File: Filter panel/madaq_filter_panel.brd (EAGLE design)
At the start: 70.6 x 38.2 mm, 34 parts

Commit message: Filter panel - V4 board (final?)
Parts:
- moved TP2 4.05 mm to (32.7, 53.3)
- moved TP1 2.61 mm to (29.0, 62.5)
- moved C6 2.43 mm to (62.6, 61.4)
- moved R1 2.04 mm to (62.6, 58.8)
- moved C5 1.84 mm to (62.7, 56.2)
- moved JP4 1.84 mm to (35.6, 57.4)
- moved JP3 1.72 mm to (32.6, 57.4)
- moved R2 1.65 mm to (62.7, 53.6)
- moved JP2 1.61 mm to (20.7, 57.4)
- moved JP1 1.52 mm to (23.9, 57.4)
- moved JP6 1.41 mm to (45.5, 57.4)
- moved TP3 1.41 mm to (39.6, 53.3)
- moved JP5 1.41 mm to (42.3, 57.4)
- moved BNC_3 0.91 mm to (24.3, 45.0)
- moved BNC_2 0.77 mm to (60.7, 45.0)
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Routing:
- net N$7: track 13.9 -> 21.3 mm
- net DAC_1: track 100.5 -> 95.1 mm
- net IN-4_B: track 11.1 -> 8.39 mm
- net -5V: track 35.9 -> 38.1 mm
- net IN-1_A: track 11.0 -> 9.06 mm
- net IN-0_A: track 11.0 -> 9.18 mm
- net SW_COM: track 41.5 -> 43.1 mm
- net SIG_1: track 22.0 -> 23.5 mm
- net GND: track 0.00 -> 1.39 mm
- net N$9: track 6.12 -> 7.50 mm
- net IN-2_A: track 8.75 -> 7.50 mm
- net DAC_2: track 3.38 -> 4.58 mm
- net SIG_2: track 32.5 -> 31.4 mm
- net N$8: track 12.4 -> 13.5 mm
- net N$3: track 8.24 -> 9.09 mm
- added copper zone on layer 16, net GND
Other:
- board size 70.6 x 38.2 mm -> 71.1 x 38.2 mm
- board text added: "2015"
- board text added: "DAC2"
- board text added: "DBG"
- board text added: "EXT"
- board text added: "IN0"
- board text added: "IN1"
- board text added: "IN2"
- board text added: "IN4"
- board text added: "INT"

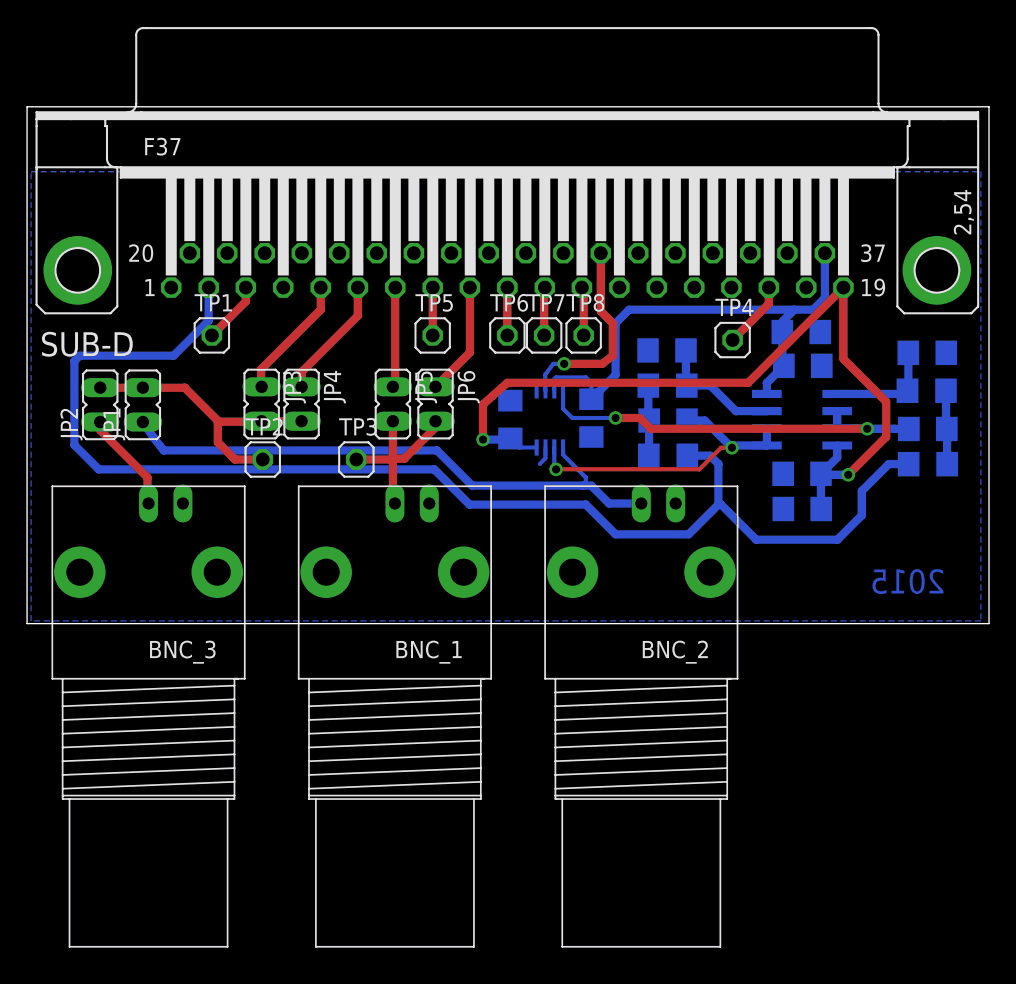
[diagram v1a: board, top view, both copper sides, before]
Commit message: Filter panel - V4 sch + brd, Robi és János átnézte - ez nem a megrendelt verzió (János még babrált a board-on)
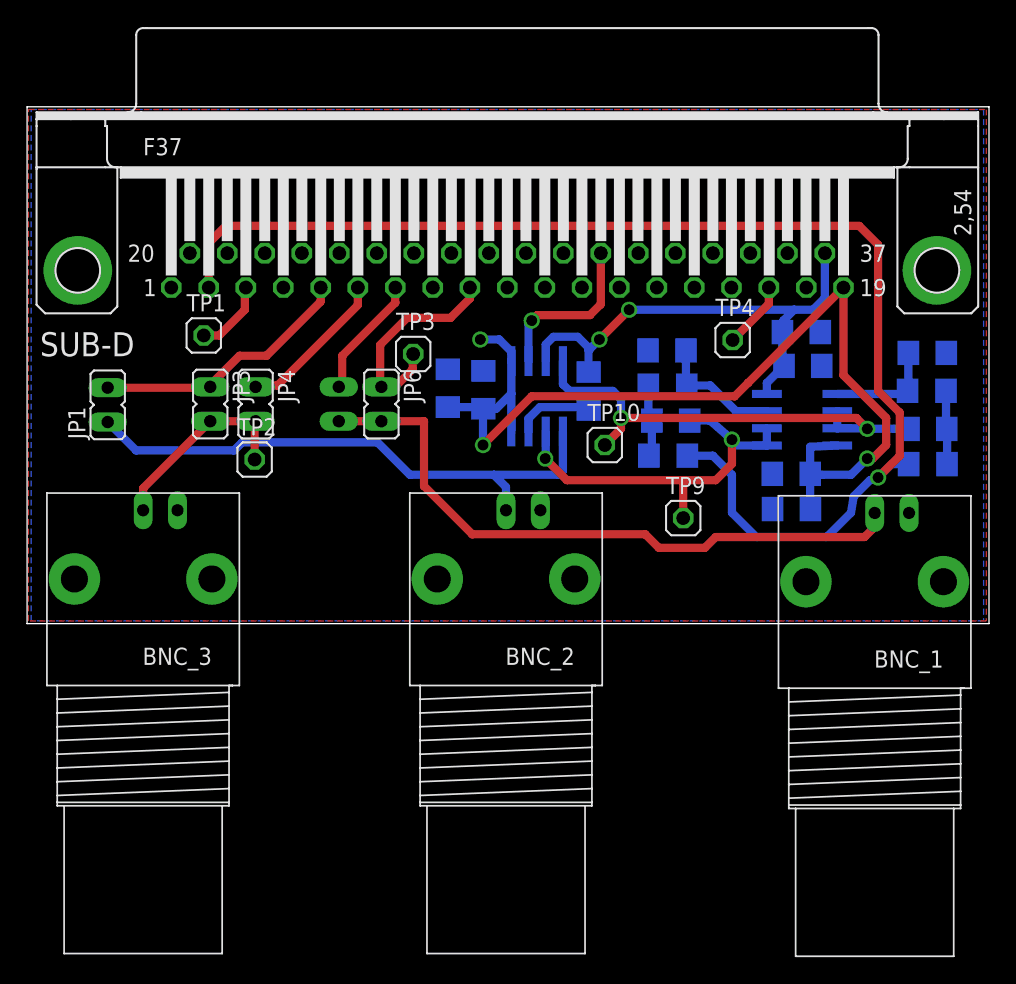
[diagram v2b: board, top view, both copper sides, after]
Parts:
- removed JP2: (no value), jumper:JP1
- removed SWITCH: TS12A12511, Zoli2_2015-02-22:MSOP08
- removed TP5, TP6, TP7, TP8: TP, MRobi:JP1
- added C11: 0.1 uF, Zoli2_2015-01-28:C1206
- added IC1: (no value), MRobi:SO08
- added TP10, TP9: TP, MRobi:JP1
- moved BNC_1 35.5 mm to (78.0, 44.3)
- moved BNC_2 10.0 mm to (50.7, 44.5)
- moved TP3 8.86 mm to (43.8, 61.1)
- moved JP5 4.00 mm to (38.3, 57.4), flipped to the bottom
- moved JP6 4.00 mm to (41.5, 57.4)
- moved JP3 3.80 mm to (28.8, 57.4)
- moved JP4 3.40 mm to (32.2, 57.4)
- moved C9 2.97 mm to (49.0, 58.5)
- moved JP1 2.60 mm to (21.3, 57.4)
- moved C10 2.01 mm to (56.8, 58.4)
- moved C1 0.80 mm to (71.8, 49.7)
- moved C2 0.80 mm to (71.8, 52.3)
- moved BNC_3 0.64 mm to (23.9, 44.5)
- moved TP1 0.60 mm to (28.4, 62.5)
- moved TP2 0.60 mm to (32.1, 53.3)
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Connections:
- removed net N$2: SWITCH.5
- removed net N$7: JP1.2, JP2.2, JP3.2, JP4.2, TP2.1
- net +5V: now also C11.2, IC1.4, IC1.5; no longer SWITCH.4
- net -5V: now also IC1.7; no longer SWITCH.7
- net GND: now also C11.1, IC1.3; no longer SWITCH.3
- net IN-0_A: now also JP1.2
- net IN-3_A: no longer TP5.1
- net IN-4_B: now also TP3.1
- net IN-5_B: no longer TP6.1
- net IN-6_B: no longer TP7.1
- net IN-7_B: no longer TP8.1
- net N$8: no longer TP3.1
- net N$9: now also JP3.2, JP4.2, TP2.1; no longer JP2.1
- net SIG_1: now also IC1.2, TP9.1; no longer SWITCH.2
- net SIG_2: now also IC1.8, TP10.1; no longer SWITCH.8
- net SW_CNTRL: now also IC1.6; no longer SWITCH.6
- net SW_COM: now also IC1.1; no longer SWITCH.1
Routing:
- net N$8: track 13.5 -> 48.0 mm
- net N$7: track 21.3 -> 0.00 mm
- net +5V: track 60.6 -> 74.0 mm, vias 2 -> 3
- net IN-0_A: track 9.18 -> 19.5 mm
- net IN-4_B: track 8.39 -> 16.0 mm
- net N$9: track 7.50 -> 14.8 mm
- net SIG_1: track 23.5 -> 29.4 mm
- net GND: track 1.39 -> 5.84 mm
- net SIG_2: track 31.4 -> 35.8 mm
- net IN-7_B: track 3.59 -> 0.00 mm
- net IN-6_B: track 3.56 -> 0.00 mm
- net IN-3_A: track 3.54 -> 0.00 mm
- net IN-5_B: track 3.54 -> 0.00 mm
- net IN-1_A: track 9.06 -> 11.4 mm
- net SW_CNTRL: track 14.7 -> 12.5 mm
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- added copper zone on layer 1, net GND
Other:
- board text added: "IN"
- board text added: "LP1"
- board text added: "LP2"
- board text added: "OUT"
- board text removed: "2015"

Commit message: Filter panel - János upgraded version, R C értékek még kellenek
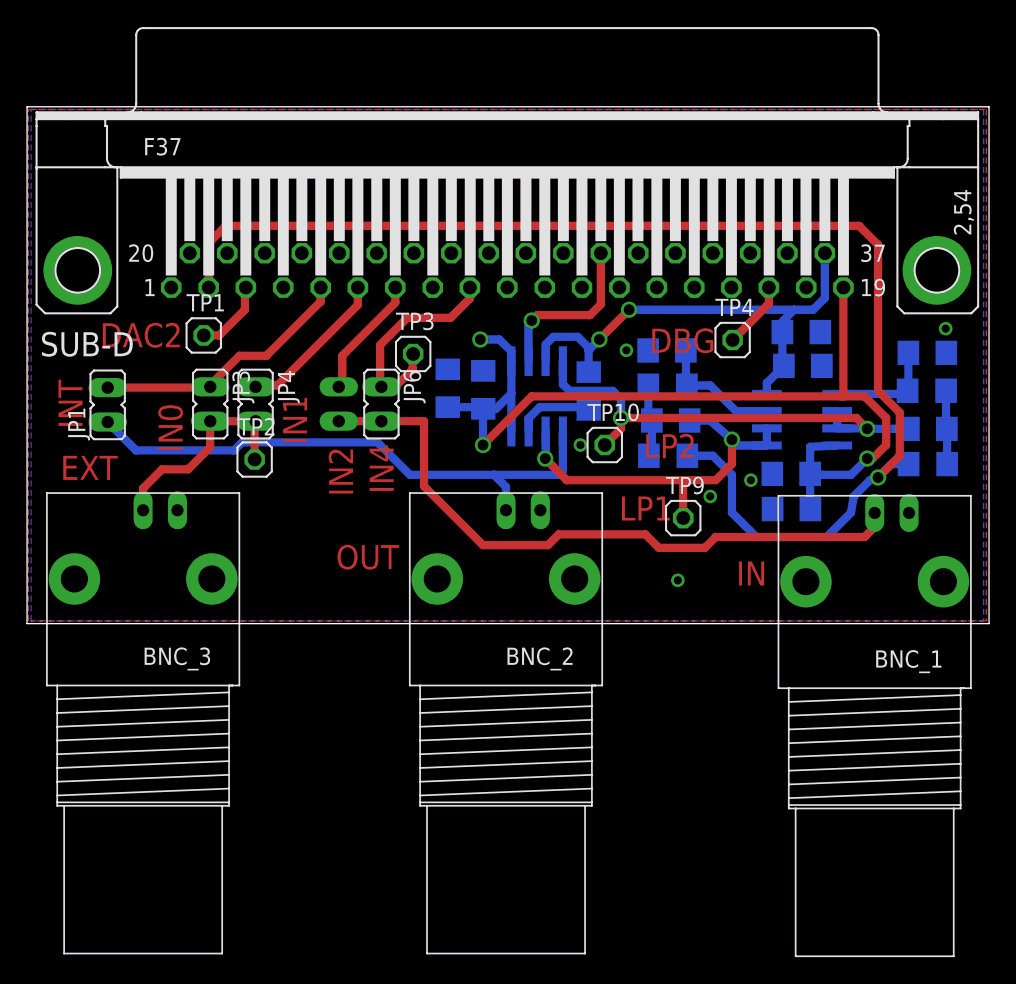
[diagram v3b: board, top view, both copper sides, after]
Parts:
- C1, C2, C3, C4: value (none) -> 100n
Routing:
- net +5V: track 74.0 -> 71.6 mm
- net N$9: track 14.8 -> 16.0 mm
- net N$8: track 48.0 -> 48.6 mm
- net GND: vias 0 -> 6
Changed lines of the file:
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@@
 <wire x1="86.4" y1="41.2" x2="86.4" y2="79.4" width="0" layer="20"/>
 <wire x1="15.3" y1="79.4" x2="15.3" y2="41.2" width="0" layer="20"/>
-<text x="26.8" y="63.4" size="1.778" layer="49" font="vector" rot="R180">DAC2</text>
-<text x="19.4" y="55.6" size="1.778" layer="49" font="vector" rot="R90">INT</text>
-<text x="26.8" y="55.4" size="1.778" layer="49" font="vector" rot="R90">IN0</text>
-<text x="35.8" y="55.6" size="1.778" layer="49" font="vector" rot="R90">IN1</text>
-<text x="39.4" y="60.4" size="1.778" layer="49" font="vector" rot="R90">IN2</text>
-<text x="66.2" y="63" size="1.778" layer="49" font="vector" rot="R180">DBG</text>
-<text x="42.4" y="60.4" size="1.778" layer="49" font="vector" rot="R90">IN4</text>
-<text x="22" y="53.6" size="1.778" layer="49" font="vector" rot="R180">EXT</text>
-<text x="73.4" y="53" size="1.778" layer="49" font="vector" rot="R180">IN</text>
-<text x="48.8" y="53.4" size="1.778" layer="49" font="vector" rot="R180">OUT</text>
+<text x="26.8" y="63.4" size="1.778" layer="1" font="vector" rot="R180">DAC2</text>
+<text x="19.4" y="55.6" size="1.778" layer="1" font="vector" rot="R90">INT</text>
+<text x="26.8" y="53.8" size="1.778" layer="1" font="vector" rot="R90">IN0</text>
+<text x="36" y="54.4" size="1.778" layer="1" font="vector" rot="R90">IN1</text>
+<text x="39.4" y="50.6" size="1.778" layer="1" font="vector" rot="R90">IN2</text>
+<text x="66.2" y="63" size="1.778" layer="1" font="vector" rot="R180">DBG</text>
+<text x="42.4" y="50.8" size="1.778" layer="1" font="vector" rot="R90">IN4</text>
+<text x="22" y="53.6" size="1.778" layer="1" font="vector" rot="R180">EXT</text>
+<text x="70" y="45.8" size="1.778" layer="1" font="vector" rot="R180">IN</text>
+<text x="42.8" y="47" size="1.778" layer="1" font="vector" rot="R180">OUT</text>
 <wire x1="15.3" y1="79.4" x2="86.4" y2="79.4" width="0" layer="20"/>
-<text x="64.8" y="55.2" size="1.778" layer="49" font="vector" rot="R180">LP2</text>
-<text x="66.8" y="47.4" size="1.778" layer="49" font="vector" rot="R180">LP1</text>
+<text x="64.8" y="55.2" size="1.778" layer="1" font="vector" rot="R180">LP2</text>
+<text x="63" y="50.6" size="1.778" layer="1" font="vector" rot="R180">LP1</text>
 </plain>
 <attributes>
@@
 <element name="BNC_2" library="Zoli2_2015-01-28" package="BNCPCB90I" value="" x="50.7" y="44.5" rot="R180"/>
 <element name="BNC_3" library="Zoli2_2015-01-28" package="BNCPCB90I" value="" x="23.88" y="44.5" rot="R180"/>
-<element name="C1" library="Zoli2_2015-01-28" package="C1206" value="" x="71.8" y="49.67" rot="MR180"/>
+<element name="C1" library="Zoli2_2015-01-28" package="C1206" value="100n" x="71.8" y="49.67" rot="MR180"/>
 <element name="C10" library="Zoli2_2015-01-28" package="C1206" value="0.1 uF" x="56.81" y="58.39" rot="MR90"/>
-<element name="C2" library="Zoli2_2015-01-28" package="C1206" value="" x="71.78" y="52.27" rot="MR180"/>
-<element name="C3" library="Zoli2_2015-01-28" package="C1206" value="" x="72.53" y="62.75" rot="MR180"/>
-<element name="C4" library="Zoli2_2015-01-28" package="C1206" value="" x="72.64" y="60.25" rot="MR180"/>
+<element name="C2" library="Zoli2_2015-01-28" package="C1206" value="100n" x="71.78" y="52.27" rot="MR180"/>
+<element name="C3" library="Zoli2_2015-01-28" package="C1206" value="100n" x="72.53" y="62.75" rot="MR180"/>
+<element name="C4" library="Zoli2_2015-01-28" package="C1206" value="100n" x="72.64" y="60.25" rot="MR180"/>
 <element name="C5" library="Zoli2_2015-01-28" package="C1206" value="" x="62.88" y="56.21" rot="MR0"/>
 <element name="C6" library="Zoli2_2015-01-28" package="C1206" value="" x="62.6" y="61.39" rot="MR180"/>
@@
 <wire x1="53.2" y1="57.2" x2="56.6" y2="57.2" width="0.6096" layer="16"/>
 <wire x1="56.6" y1="57.2" x2="56.81" y2="56.99" width="0.6096" layer="16"/>
-<polygon width="0.6096" layer="16" isolate="0.3048">
+<polygon width="0.6096" layer="16" isolate="0.4064">
 <vertex x="15.6" y="79.2"/>
 <vertex x="86" y="79.2"/>
@@
 <vertex x="15.6" y="41.4"/>
 </polygon>
-<polygon width="0.4064" layer="1" isolate="0.3048">
+<polygon width="0.4064" layer="1" isolate="0.4064">
 <vertex x="15.4" y="79.2"/>
 <vertex x="86.2" y="79.2"/>
@@
 <vertex x="15.4" y="41.4"/>
 </polygon>
+<via x="65.8" y="50.6" extent="1-16" drill="0.6" shape="octagon"/>
+<via x="68.8" y="51.8" extent="1-16" drill="0.6" shape="octagon"/>
+<via x="56.2" y="54.4" extent="1-16" drill="0.6" shape="octagon"/>
+<via x="59.6" y="61.4" extent="1-16" drill="0.6" shape="octagon"/>
+<via x="63.4" y="44.4" extent="1-16" drill="0.6" shape="octagon"/>
+<via x="83.2" y="63" extent="1-16" drill="0.6" shape="octagon"/>
 </signal>
 <signal name="N$4">
@@
 <wire x1="74.05" y1="52.2" x2="73.18" y2="52.27" width="0.6096" layer="16"/>
 <via x="48.8" y="62.2" extent="1-16" drill="0.8" shape="octagon"/>
-<wire x1="68.6012" y1="59" x2="75.6412" y2="66.04" width="0.6096" layer="1"/>
 <wire x1="78.8" y1="56.4" x2="78.8" y2="54.4" width="0.6096" layer="1"/>
 <wire x1="74.05" y1="52.2" x2="76.2" y2="52.2" width="0.6096" layer="16"/>
@@
 <wire x1="49.02" y1="57.08" x2="49.975" y2="57.08" width="0.6096" layer="16"/>
 <wire x1="49.975" y1="57.08" x2="51.095" y2="58.2" width="0.6096" layer="16"/>
-<wire x1="68.6012" y1="59" x2="68.6" y2="59" width="0.6096" layer="1"/>
-<wire x1="68.6" y1="59" x2="67.6" y2="58" width="0.6096" layer="1"/>
-<wire x1="67.6" y1="58" x2="52.6" y2="58" width="0.6096" layer="1"/>
 <wire x1="52.6" y1="58" x2="49" y2="54.4" width="0.6096" layer="1"/>
 <via x="49" y="54.4" extent="1-16" drill="0.8" shape="octagon"/>
@@
 <wire x1="77.4" y1="53.4" x2="77.8" y2="53.4" width="0.6096" layer="1"/>
 <wire x1="77.8" y1="53.4" x2="78.8" y2="54.4" width="0.6096" layer="1"/>
-<wire x1="75.6412" y1="66.04" x2="75.6412" y2="59.5588" width="0.6096" layer="1"/>
-<wire x1="75.6412" y1="59.5588" x2="78.8" y2="56.4" width="0.6096" layer="1"/>
+<wire x1="75.6412" y1="66.04" x2="75.6412" y2="58" width="0.6096" layer="1"/>
+<wire x1="52.6" y1="58" x2="75.4" y2="58" width="0.6096" layer="1"/>
+<wire x1="75.4" y1="58" x2="75.6412" y2="58" width="0.6096" layer="1"/>
+<wire x1="78.8" y1="56.4" x2="77.2" y2="58" width="0.6096" layer="1"/>
+<wire x1="77.2" y1="58" x2="75.6412" y2="58" width="0.6096" layer="1"/>
 </signal>
 <signal name="DAC_1">
@@
 <wire x1="41.49" y1="56.16" x2="44.64" y2="56.16" width="0.6096" layer="1"/>
 <wire x1="44.64" y1="56.16" x2="44.64" y2="51.36" width="0.6096" layer="1"/>
-<wire x1="44.64" y1="51.36" x2="48.2" y2="47.8" width="0.6096" layer="1"/>
+<wire x1="44.64" y1="51.36" x2="49" y2="47" width="0.6096" layer="1"/>
 <wire x1="66.2" y1="47.6" x2="77.2" y2="47.6" width="0.6096" layer="1"/>
 <wire x1="77.2" y1="47.6" x2="77.8" y2="48.2" width="0.6096" layer="1"/>
 <wire x1="77.8" y1="48.2" x2="77.8" y2="49.23" width="0.6096" layer="1"/>
 <wire x1="77.8" y1="49.23" x2="77.95" y2="49.38" width="0.6096" layer="1"/>
-<wire x1="48.2" y1="47.8" x2="61" y2="47.8" width="0.6096" layer="1"/>
 <wire x1="61" y1="47.8" x2="62" y2="46.8" width="0.6096" layer="1"/>
 <wire x1="62" y1="46.8" x2="65.4" y2="46.8" width="0.6096" layer="1"/>
 <wire x1="65.4" y1="46.8" x2="66.2" y2="47.6" width="0.6096" layer="1"/>
+<wire x1="49" y1="47" x2="53.8" y2="47" width="0.6096" layer="1"/>
+<wire x1="53.8" y1="47" x2="54.6" y2="47.8" width="0.6096" layer="1"/>
+<wire x1="54.6" y1="47.8" x2="61" y2="47.8" width="0.6096" layer="1"/>
 </signal>
 <signal name="SIG_1">
@@
 <wire x1="28.84" y1="56.16" x2="32.19" y2="56.16" width="0.6096" layer="1"/>
 <wire x1="23.88" y1="49.58" x2="23.88" y2="51.2" width="0.6096" layer="1"/>
-<wire x1="23.88" y1="51.2" x2="28.84" y2="56.16" width="0.6096" layer="1"/>
 <wire x1="32.12" y1="53.33" x2="32.12" y2="56.09" width="0.6096" layer="1"/>
 <wire x1="32.12" y1="56.09" x2="32.19" y2="56.16" width="0.6096" layer="1"/>
+<wire x1="23.88" y1="51.2" x2="25.28" y2="52.6" width="0.6096" layer="1"/>
+<wire x1="25.28" y1="52.6" x2="27.2" y2="52.6" width="0.6096" layer="1"/>
+<wire x1="27.2" y1="52.6" x2="28.84" y2="54.24" width="0.6096" layer="1"/>
+<wire x1="28.84" y1="54.24" x2="28.84" y2="56.16" width="0.6096" layer="1"/>
 </signal>
 <signal name="DAC_2">

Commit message: Souce - Filter panellel működő kód - P1_3 filter/switch control push pull-ra állítva - kimeneti jel DAC0 helyett DAC1-en megy - @1, @2 adc ch config utasítások
Labview
- több periódust is lehet használni
- optimális izé képletek korrigálva (period <--> samples)

Filter panel
- R,C értékek belőve, megépített verzió
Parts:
- C10, C11, C12: value 0.1 uF -> 100n
- C2, C4: value 100n -> 10u
- renumbered C9 to C12
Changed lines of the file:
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@@
 <element name="BNC_3" library="Zoli2_2015-01-28" package="BNCPCB90I" value="" x="23.88" y="44.5" rot="R180"/>
 <element name="C1" library="Zoli2_2015-01-28" package="C1206" value="100n" x="71.8" y="49.67" rot="MR180"/>
-<element name="C10" library="Zoli2_2015-01-28" package="C1206" value="0.1 uF" x="56.81" y="58.39" rot="MR90"/>
-<element name="C2" library="Zoli2_2015-01-28" package="C1206" value="100n" x="71.78" y="52.27" rot="MR180"/>
+<element name="C10" library="Zoli2_2015-01-28" package="C1206" value="100n" x="56.81" y="58.39" rot="MR90"/>
+<element name="C2" library="Zoli2_2015-01-28" package="C1206" value="10u" x="71.78" y="52.27" rot="MR180"/>
 <element name="C3" library="Zoli2_2015-01-28" package="C1206" value="100n" x="72.53" y="62.75" rot="MR180"/>
-<element name="C4" library="Zoli2_2015-01-28" package="C1206" value="100n" x="72.64" y="60.25" rot="MR180"/>
+<element name="C4" library="Zoli2_2015-01-28" package="C1206" value="10u" x="72.64" y="60.25" rot="MR180"/>
 <element name="C5" library="Zoli2_2015-01-28" package="C1206" value="" x="62.88" y="56.21" rot="MR0"/>
 <element name="C6" library="Zoli2_2015-01-28" package="C1206" value="" x="62.6" y="61.39" rot="MR180"/>
 <element name="C7" library="Zoli2_2015-01-28" package="C1206" value="" x="81.88" y="55.59" rot="MR180"/>
 <element name="C8" library="Zoli2_2015-01-28" package="C1206" value="" x="81.84" y="61.21" rot="MR0"/>
-<element name="C9" library="Zoli2_2015-01-28" package="C1206" value="0.1 uF" x="49.02" y="58.48" rot="MR270"/>
+<element name="C12" library="Zoli2_2015-01-28" package="C1206" value="100n" x="49.02" y="58.48" rot="MR270"/>
 <element name="JP1" library="jumper" package="JP1" value="" x="21.26" y="57.37"/>
 <element name="JP3" library="jumper" package="JP1" value="" x="28.84" y="57.43" rot="R180"/>
@@
 <element name="TP4" library="MRobi" package="JP1" value="TP" x="67.45" y="62.16"/>
 <element name="IC1" library="MRobi" package="SO08" value="" x="53" y="58" rot="MR0"/>
-<element name="C11" library="Zoli2_2015-01-28" package="C1206" value="0.1 uF" x="46.4" y="58.6" rot="MR270"/>
+<element name="C11" library="Zoli2_2015-01-28" package="C1206" value="100n" x="46.4" y="58.6" rot="MR270"/>
 <element name="TP9" library="MRobi" package="JP1" value="TP" x="63.8" y="49"/>
 <element name="TP10" library="MRobi" package="JP1" value="TP" x="58" y="54.4"/>
@@
 <contactref element="C1" pad="1"/>
 <contactref element="C10" pad="1"/>
-<contactref element="C9" pad="1"/>
+<contactref element="C12" pad="1"/>
 <contactref element="BNC_3" pad="SHIELD"/>
 <contactref element="BNC_1" pad="SHIELD"/>
@@
 <wire x1="76.2" y1="52.2" x2="77.4" y2="53.4" width="0.6096" layer="16"/>
 <contactref element="IC1" pad="5"/>
-<contactref element="C9" pad="2"/>
+<contactref element="C12" pad="2"/>
 <contactref element="IC1" pad="4"/>
 <contactref element="C11" pad="2"/>
